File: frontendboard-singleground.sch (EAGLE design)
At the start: 64 parts, among them U1 MAX2769, X3 BU-SMA-H

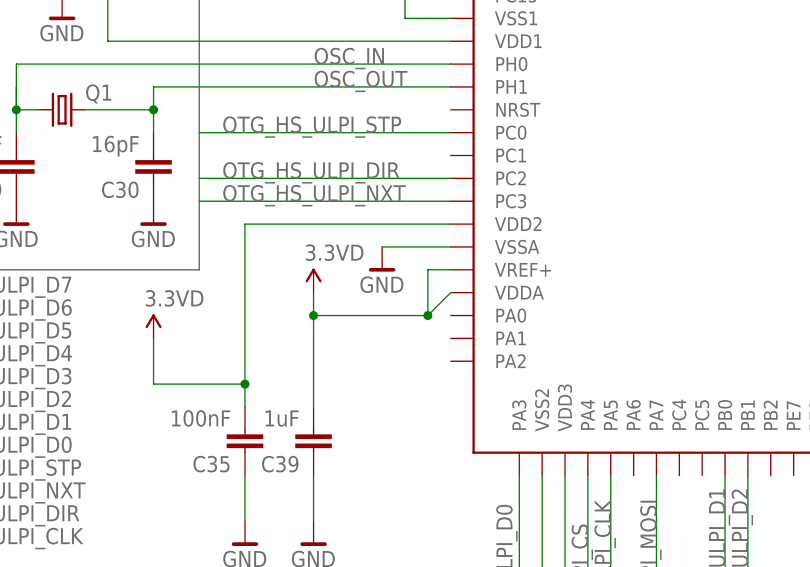
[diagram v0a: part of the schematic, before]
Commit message: Change layout for MAX2769 chip. RF header needs pin swap.
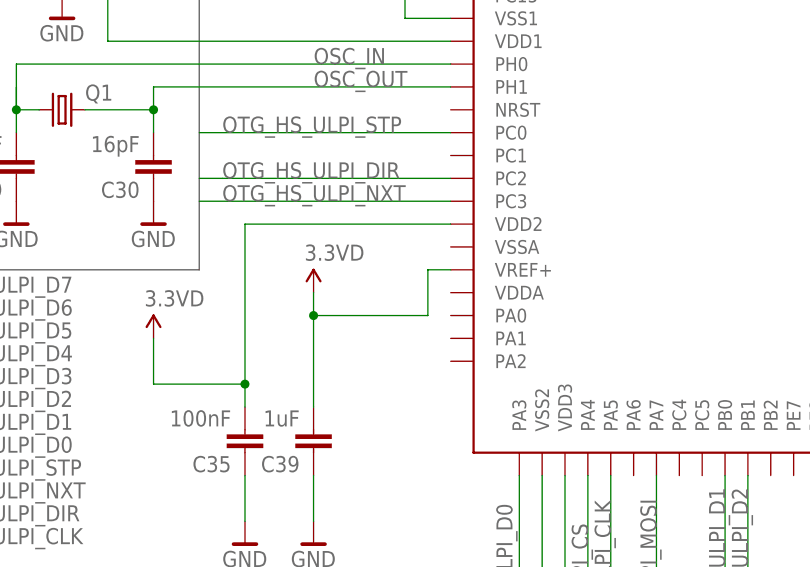
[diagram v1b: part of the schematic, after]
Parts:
- C1, C2, C20, C23, C26, C27, C28, C29, C30, C31, C33, C34, C35, C36, C37, C38, C39: device rcl_custom:C-EU0603-B -> rcl:C-EUC0402
- L2: device rcl_custom:L-US0603-B -> rcl_custom:L-US0402-A
- R1, R10, R7, R8, R9: device rcl_custom:R-US_0603-B -> rcl:R-US_R0402
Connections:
- net 3.3VD: no longer U$3.VDDA
- net BAR_GND: no longer U$3.VSSA

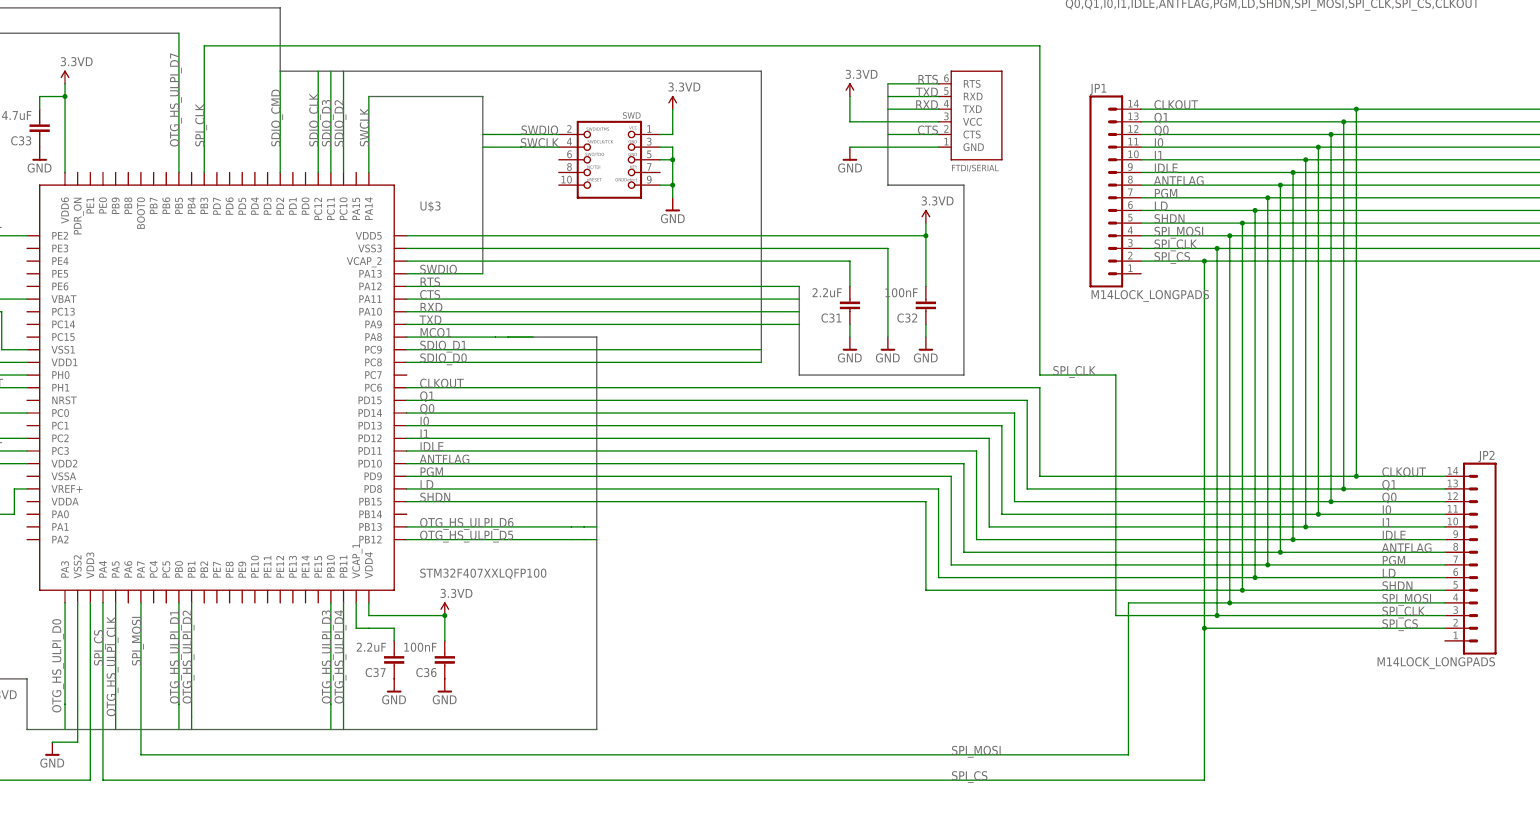
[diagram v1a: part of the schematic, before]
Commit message: RF side signals routed except for power.
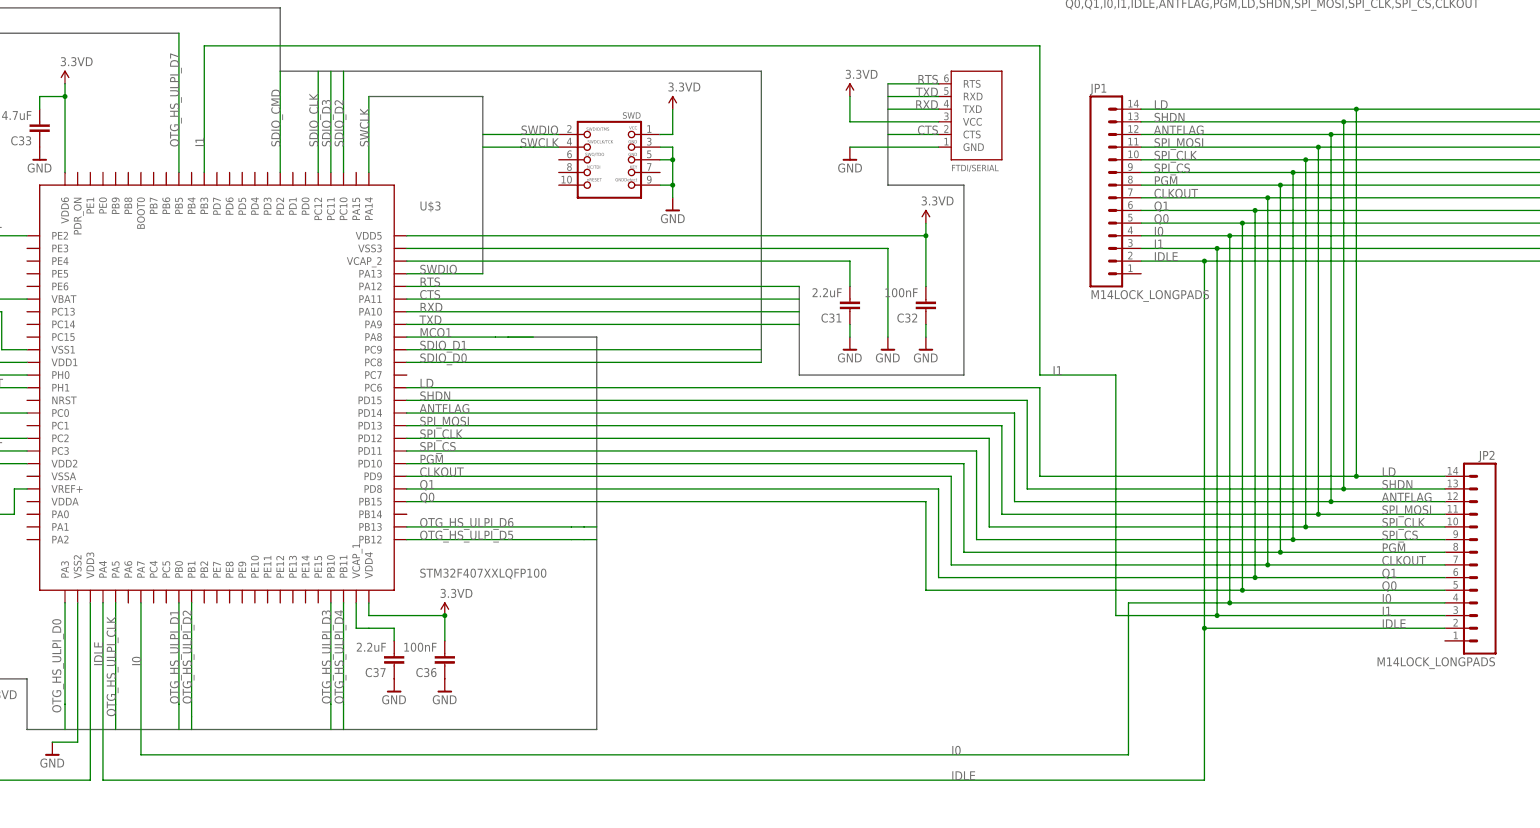
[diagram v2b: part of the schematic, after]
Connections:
- net ANTFLAG: now also JP1.12, JP2.12, U$3.PD14; no longer JP1.8, JP2.8, U$3.PD10
- net CLKOUT: now also JP1.7, JP2.7, U$3.PD9; no longer JP1.14, JP2.14, U$3.PC6
- net I0: now also JP1.4, JP2.4, U$3.PA7; no longer JP1.11, JP2.11, U$3.PD13
- net I1: now also JP1.3, JP2.3, U$3.PB3; no longer JP1.10, JP2.10, U$3.PD12
- net IDLE: now also JP1.2, JP2.2, U$3.PA4; no longer JP1.9, JP2.9, U$3.PD11
- net LD: now also JP1.14, JP2.14, U$3.PC6; no longer JP1.6, JP2.6, U$3.PD8
- net PGM: now also JP1.8, JP2.8, U$3.PD10; no longer JP1.7, JP2.7, U$3.PD9
- net Q0: now also JP1.5, JP2.5, U$3.PB15; no longer JP1.12, JP2.12, U$3.PD14
- net Q1: now also JP1.6, JP2.6, U$3.PD8; no longer JP1.13, JP2.13, U$3.PD15
- net SHDN: now also JP1.13, JP2.13, U$3.PD15; no longer JP1.5, JP2.5, U$3.PB15
- net SPI_CLK: now also JP1.10, JP2.10, U$3.PD12; no longer JP1.3, JP2.3, U$3.PB3
- net SPI_CS: now also JP1.9, JP2.9, U$3.PD11; no longer JP1.2, JP2.2, U$3.PA4
- net SPI_MOSI: now also JP1.11, JP2.11, U$3.PD13; no longer JP1.4, JP2.4, U$3.PA7

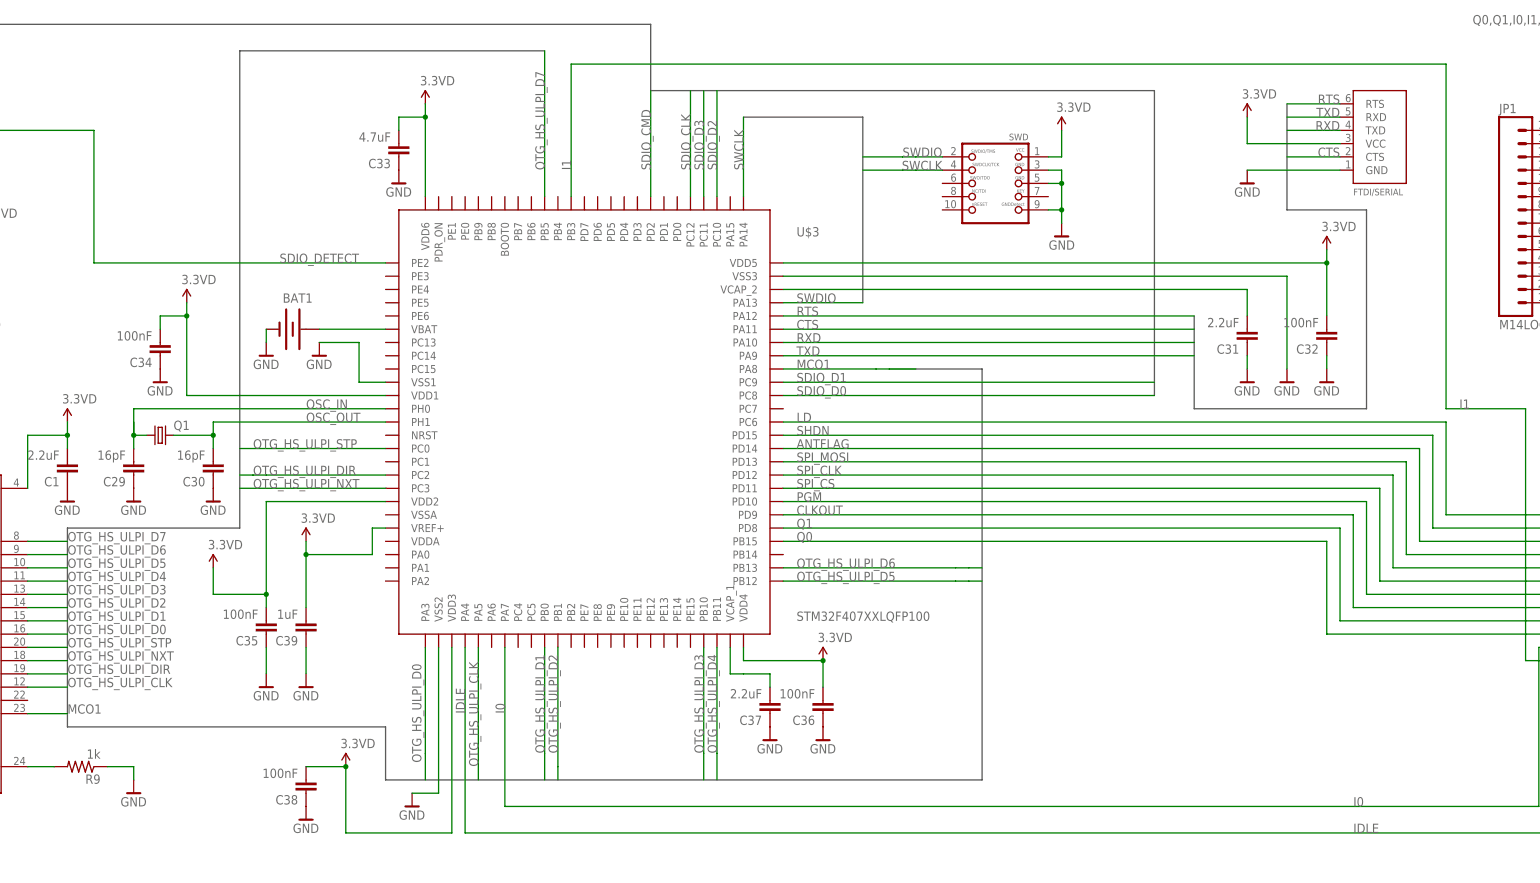
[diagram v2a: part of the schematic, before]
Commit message: Fixed reversed P26,P28 reversed on STM32F4. Better layout on digital side. Incomplete.
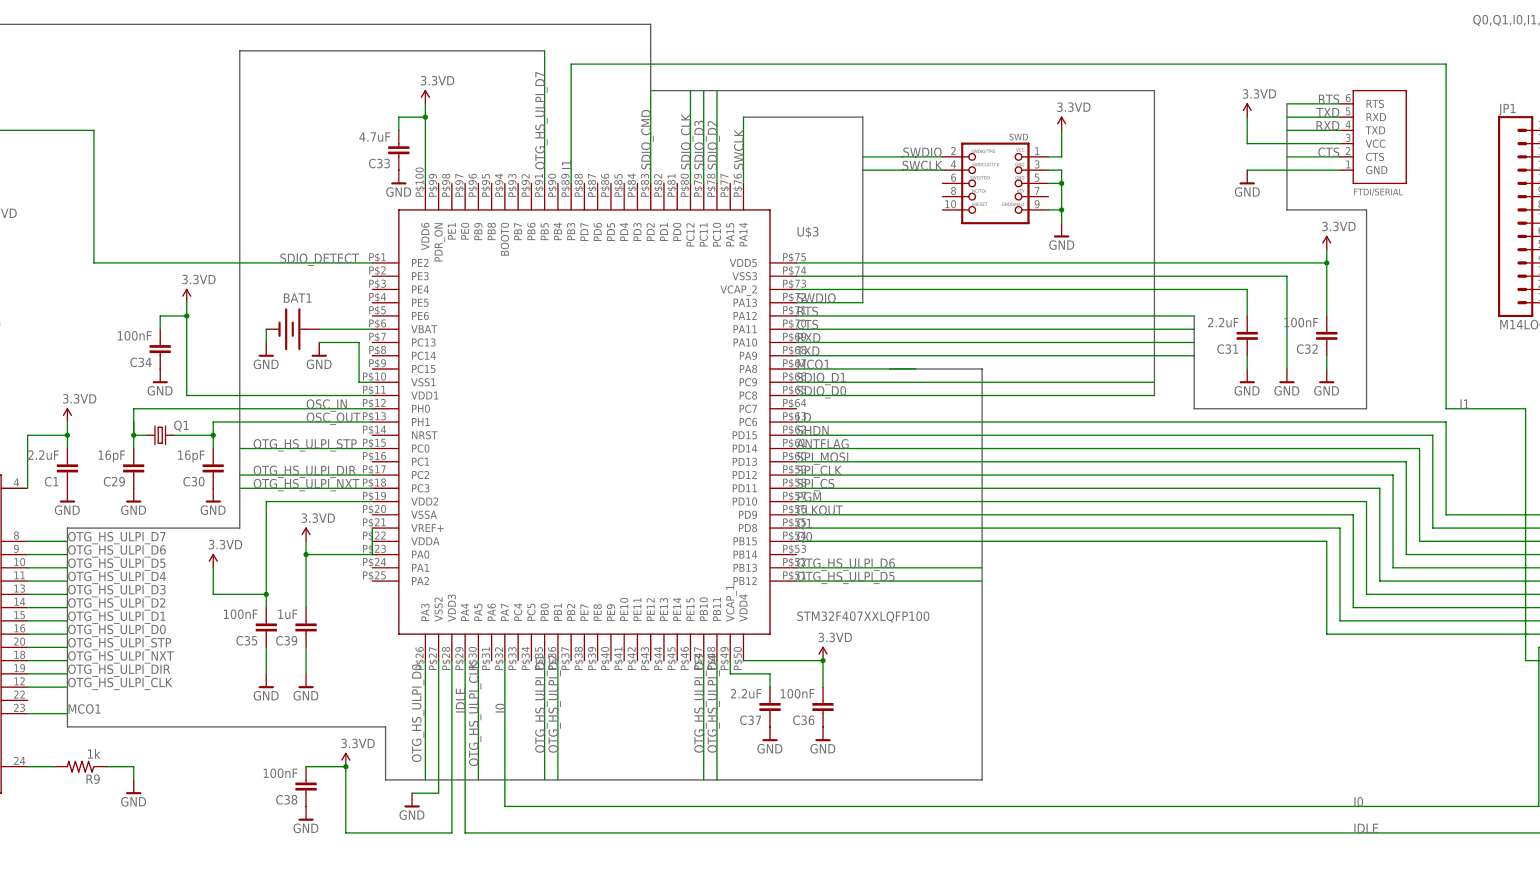
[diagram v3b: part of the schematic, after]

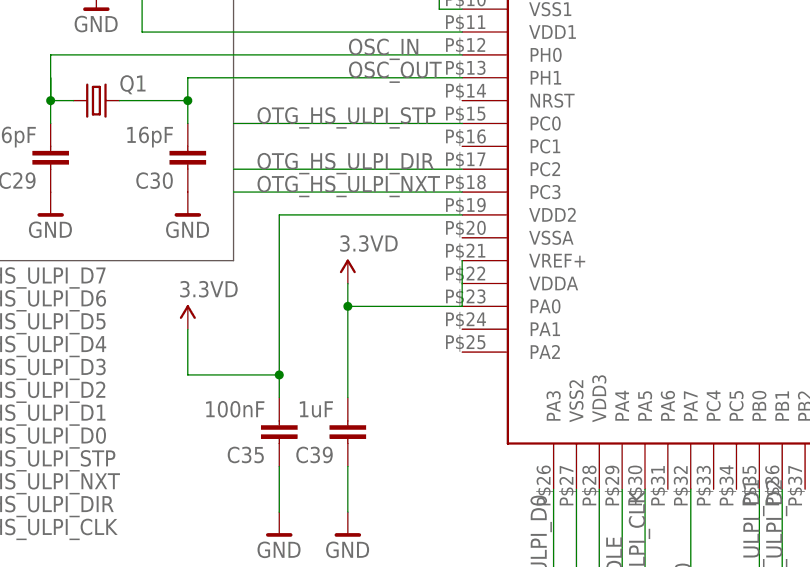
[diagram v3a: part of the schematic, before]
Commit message: Layout done and verified. Fails Laen's DRU for layer setup issues.
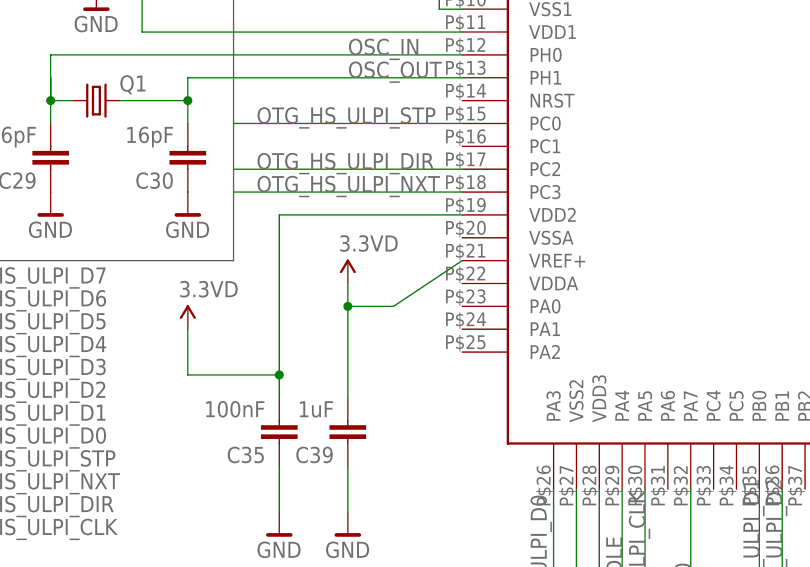
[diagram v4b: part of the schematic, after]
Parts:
- C32: device rcl_custom:C-EU0603-B -> rcl:C-EUC0402
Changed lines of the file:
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@@
 <part name="DIG_GND45" library="supply" deviceset="GND_BAR" device="" value="GND"/>
 <part name="DIG_GND46" library="supply" deviceset="GND_BAR" device="" value="GND"/>
-<part name="C32" library="rcl_custom" deviceset="C-EU" device="0603-B" value="100nF"/>
+<part name="C32" library="rcl" deviceset="C-EU" device="C0402" value="100nF"/>
 <part name="C33" library="rcl" deviceset="C-EU" device="C0402" value="4.7uF"/>
 <part name="DIG_GND47" library="supply" deviceset="GND_BAR" device="" value="GND"/>
@@
 <instance part="DIG_GND45" gate="1" x="396.24" y="116.84"/>
 <instance part="DIG_GND46" gate="1" x="411.48" y="116.84"/>
-<instance part="C32" gate="CE" x="411.48" y="124.46" rot="R180"/>
+<instance part="C32" gate="G$1" x="411.48" y="124.46" rot="R180"/>
 <instance part="C33" gate="G$1" x="233.68" y="160.02" rot="R180"/>
 <instance part="DIG_GND47" gate="1" x="233.68" y="154.94"/>
@@
 <segment>
 <pinref part="DIG_GND46" gate="1" pin="BAR_GND"/>
-<pinref part="C32" gate="CE" pin="1"/>
+<pinref part="C32" gate="G$1" pin="1"/>
 <wire x1="411.48" y1="119.38" x2="411.48" y2="121.92" width="0.1524" layer="91"/>
 </segment>
@@
 <wire x1="309.88" y1="139.7" x2="411.48" y2="139.7" width="0.1524" layer="91"/>
 <wire x1="411.48" y1="139.7" x2="411.48" y2="129.54" width="0.1524" layer="91"/>
-<pinref part="C32" gate="CE" pin="2"/>
+<pinref part="C32" gate="G$1" pin="2"/>
 <wire x1="411.48" y1="139.7" x2="411.48" y2="142.24" width="0.1524" layer="91"/>
 <junction x="411.48" y="139.7"/>
@@
 </segment>
 <segment>
-<wire x1="215.9" y1="83.82" x2="228.6" y2="83.82" width="0.1524" layer="91"/>
+<wire x1="215.9" y1="83.82" x2="220.98" y2="83.82" width="0.1524" layer="91"/>
 <wire x1="215.9" y1="83.82" x2="215.9" y2="86.36" width="0.1524" layer="91"/>
 <pinref part="C39" gate="G$1" pin="2"/>
 <wire x1="215.9" y1="83.82" x2="215.9" y2="73.66" width="0.1524" layer="91"/>
 <pinref part="U$3" gate="G$1" pin="VREF+"/>
-<wire x1="228.6" y1="88.9" x2="228.6" y2="83.82" width="0.1524" layer="91"/>
+<wire x1="228.6" y1="88.9" x2="220.98" y2="83.82" width="0.1524" layer="91"/>
 <junction x="215.9" y="83.82"/>
 <pinref part="U$18" gate="3.3VD" pin="3.3VD"/>
@@
 </sheet>
 </sheets>
-<errors>
-</errors>
 </schematic>
 </drawing>
